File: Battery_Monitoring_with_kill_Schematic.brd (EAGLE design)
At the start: 50.8 x 127 mm, 57 parts, among them CON4 MOLEX_5566-2, CON5 S3B-PH-SM4-TB, CON6 S3B-PH-SM4-TB, U1 INA3221., U2 INA3221., U4 TEENSY_3.1_BASIC_2, U6 TCAN1042HVDR

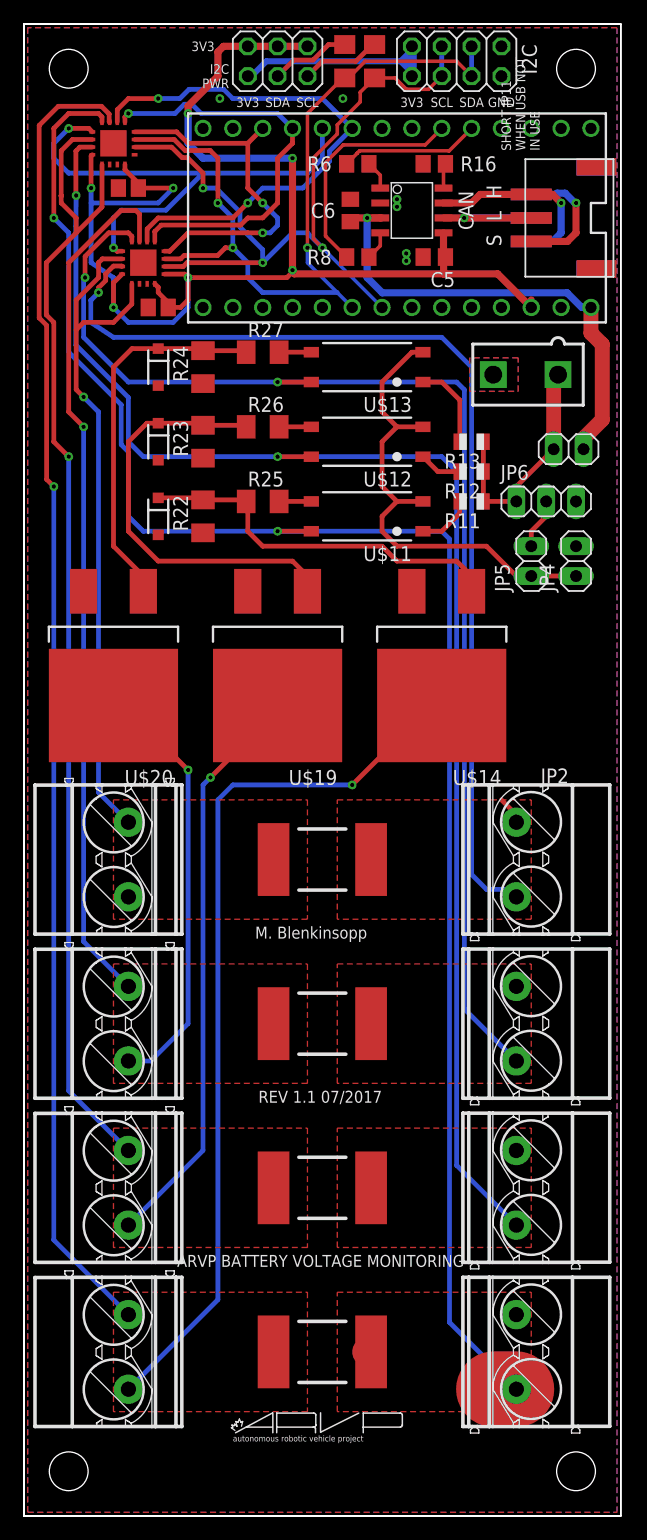
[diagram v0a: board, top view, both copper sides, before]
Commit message: Rerouted the motor and battery lines to the INA's. Changed the MOSFET drain routes.
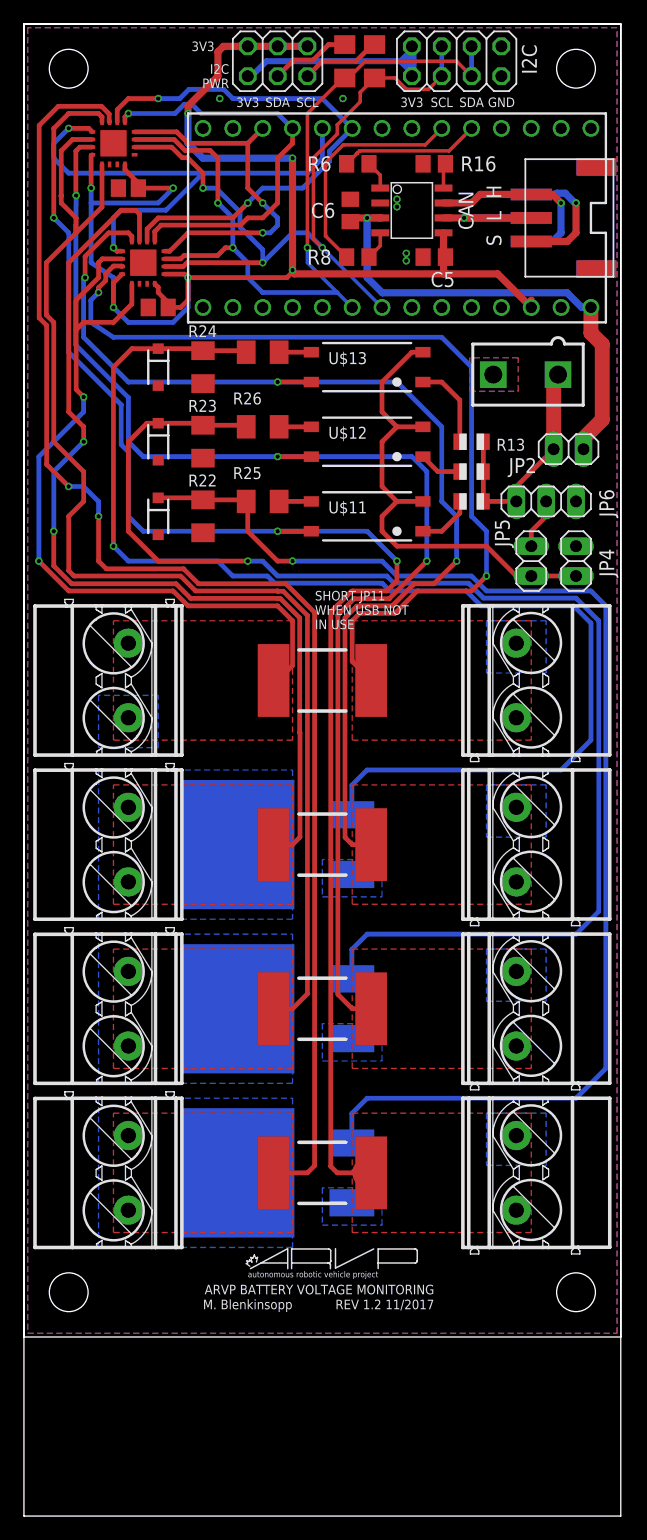
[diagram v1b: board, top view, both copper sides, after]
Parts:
- moved U$14 45.4 mm to (125.7, -11.4), flipped to the bottom, turned to 270 degrees
- moved U$19 29.2 mm to (125.7, 2.54), flipped to the bottom, turned to 270 degrees
- moved U$20 20.7 mm to (125.7, 16.5), flipped to the bottom, turned to 270 degrees
- moved R3 15.2 mm to (129.5, 16.5)
- moved R4 15.2 mm to (129.5, -11.4)
- moved U$1 15.2 mm to (146.1, -11.4)
- moved U$3 15.2 mm to (146.1, 16.5)
- moved U$5 15.2 mm to (113.0, -11.4)
- moved U$7 15.2 mm to (113.0, 16.5)
- moved R7 15.2 mm to (129.5, 30.5)
- moved U$4 15.2 mm to (146.1, 30.5)
- moved U$8 15.2 mm to (113.0, 30.5)
- moved R1 15.2 mm to (129.5, 2.54)
- moved U$2 15.2 mm to (146.1, 2.54)
- moved U$24 15.2 mm to (151.1, -21.6)
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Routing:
- net MG1: track 32.1 -> 108.4 mm, vias 0 -> 1
- net MD1: track 75.7 -> 0.00 mm, vias 1 -> 0
- net MG2: track 36.5 -> 111.2 mm, vias 0 -> 1
- net MG3: track 32.2 -> 105.1 mm, vias 0 -> 1
- net MD2: track 49.5 -> 0.00 mm, vias 1 -> 0
- net MD3: track 36.6 -> 0.00 mm, vias 1 -> 0
- net 0-26V_BATTERY1: track 148.8 -> 127.4 mm, vias 2 -> 3
- net 0-26V_BATTERY2: track 126.2 -> 110.2 mm, vias 2 -> 3
- net 0-26V_BATTERY3: track 108.4 -> 93.4 mm, vias 2 -> 3
- net 0-26V_BATTERY4: track 89.3 -> 78.6 mm, vias 1 -> 2
- net MOTOR3: track 74.0 -> 81.7 mm, vias 1 -> 2
- net MOTOR4: track 59.8 -> 67.2 mm, vias 1 -> 2
- net MOTOR2: track 99.4 -> 106.5 mm, vias 1 -> 0
- net MOTOR1: track 112.0 -> 118.6 mm, vias 1 -> 2
- net GND: track 2.70 -> 0.27 mm
- added copper zone on layer 16, net MD1
- added copper zone on layer 16, net MD2
- added copper zone on layer 16, net MD3
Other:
- outline, holes or cut-outs redrawn
- board text added: "REV 1.2 11/2017"
- board text removed: "REV 1.1 07/2017"

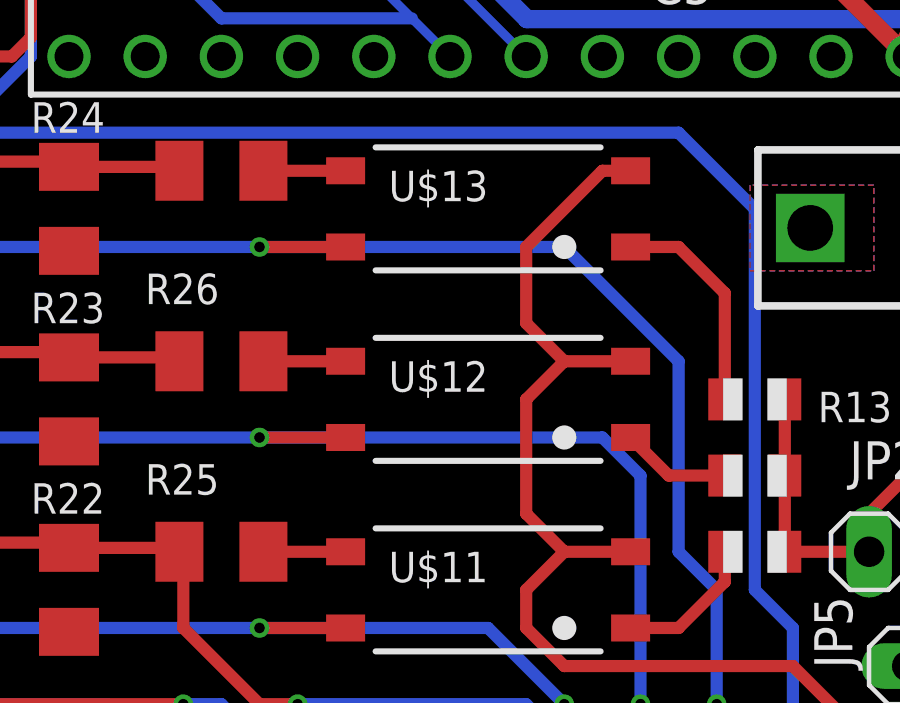
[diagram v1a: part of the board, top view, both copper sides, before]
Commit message: Added some GND VIAs
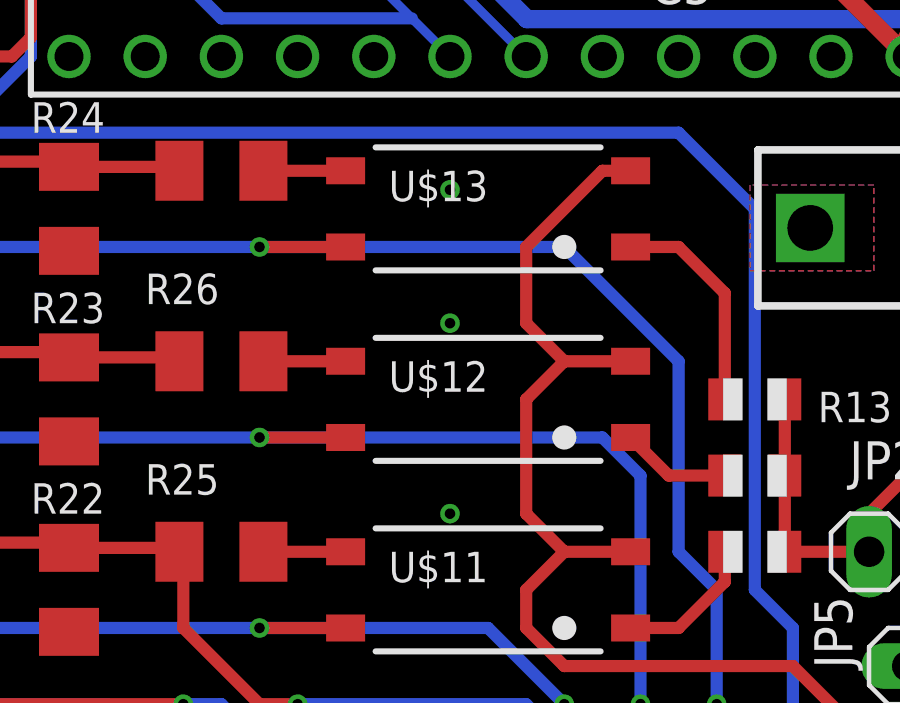
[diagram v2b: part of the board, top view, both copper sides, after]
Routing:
- net GND: vias 6 -> 9
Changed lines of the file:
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@@
 <vertex x="148.59" y="-6.35"/>
 </polygon>
+<via x="132.08" y="57.785" extent="1-16" drill="0.35"/>
+<via x="132.08" y="53.34" extent="1-16" drill="0.35"/>
+<via x="132.08" y="46.99" extent="1-16" drill="0.35"/>
 </signal>
 <signal name="VBAT1">
